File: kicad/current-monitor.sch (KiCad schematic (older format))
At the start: 4 parts, among them J1 Conn_01x02_Male, J2 Conn_01x02_Male, J3 Conn_02x05_Top_Bottom

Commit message: snapshot
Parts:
- removed J1, J2: Conn_01x02_Male, Connector_PinHeader_2.54mm:PinHeader_1x02_P2.54mm_Vertical_SMD_Pin1Left, symbol Connector:Conn_01x02_Male
- removed J3: Conn_02x05_Top_Bottom, Connector_PinHeader_2.54mm:PinHeader_2x05_P2.54mm_Vertical_SMD, symbol Connector_Generic:Conn_02x05_Top_Bottom
- added H1, H2: MountingHole, MountingHole:MountingHole_2.2mm_M2_Pad_Via, symbol Mechanical:MountingHole
- added J1, J2: Conn_02x02_Odd_Even, Connector_PinHeader_2.54mm:PinHeader_2x02_P2.54mm_Vertical_SMD, symbol Connector_Generic:Conn_02x02_Odd_Even
- added J3: Conn_02x05_Odd_Even, Connector_PinHeader_2.54mm:PinHeader_2x05_P2.54mm_Vertical_SMD, symbol Connector_Generic:Conn_02x05_Odd_Even
- added R12: 2, Resistor_SMD:R_0612_1632Metric, symbol Device:R
- R1: footprint Resistor_SMD:R_0603_1608Metric -> Resistor_SMD:R_0612_1632Metric; Description (none) -> RES SMD 2 OHM 3/4W 1206 WIDE; Digi-Key Part Number (none) -> RHM2YCT-ND; Manufacturer (none) -> Rohm Semiconductor; Manufacturer Part Number (none) -> LTR18EZPF2R00
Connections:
- net GND: now also J1.1 (Pin_1), J1.3 (Pin_3), J2.1 (Pin_1), J2.3 (Pin_3)
- net adc/3V3: now also J3.6 (Pin_6)
- net adc/CIPO: now also J3.3 (Pin_3)
- net adc/COPI: now also J3.1 (Pin_1)
- net adc/GND: now also J3.2 (Pin_2), J3.8 (Pin_8)
- net adc/SCLK: now also J3.5 (Pin_5)
- net adc/~CS: now also J3.7 (Pin_7)
- net adc/~DRDY: now also J3.9 (Pin_9)
- net adc/~SYNC: now also J3.10 (Pin_10)
- net power/5V: now also J3.4 (Pin_4)
- net sensors/S1+: now also R1.1, J1.4 (Pin_4); no longer R1.2
- net sensors/S1-: now also R1.2, J1.2 (Pin_2); no longer R1.1
- new net sensors/S3+: J2.4 (Pin_4), R12.1
- new net sensors/S3-: J2.2 (Pin_2), R12.2
- no-connect marks 2 -> 0
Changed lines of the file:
@@
 F 0 "R1" H 2320 3146 50  0000 L CNN
 F 1 "2" H 2320 3055 50  0000 L CNN
-F 2 "Resistor_SMD:R_0603_1608Metric" V 2180 3100 50  0001 C CNN
-F 3 "~" H 2250 3100 50  0001 C CNN
+F 2 "Resistor_SMD:R_0612_1632Metric" V 2180 3100 50  0001 C CNN
+F 3 "https://www.rohm.com/datasheet/LTR100JZPD/ltr-e" H 2250 3100 50  0001 C CNN
+F 4 "RHM2YCT-ND" H 2250 3100 50  0001 C CNN "Digi-Key Part Number"
+F 5 "Rohm Semiconductor" H 2250 3100 50  0001 C CNN "Manufacturer"
+F 6 "LTR18EZPF2R00" H 2250 3100 50  0001 C CNN "Manufacturer Part Number"
+F 7 "RES SMD 2 OHM 3/4W 1206 WIDE" H 2250 3100 50  0001 C CNN "Description"
 	1    2250 3100
-	1    0    0    -1
-$EndComp
-$Comp
-L Connector:Conn_01x02_Male J1
-U 1 1 5FC45001
-P 2250 2400
-F 0 "J1" V 2312 2444 50  0000 L CNN
-F 1 "Conn_01x02_Male" V 2403 2444 50  0000 L CNN
-F 2 "Connector_PinHeader_2.54mm:PinHeader_1x02_P2.54mm_Vertical_SMD_Pin1Left" H 2250 2400 50  0001 C CNN
-F 3 "~" H 2250 2400 50  0001 C CNN
-	1    2250 2400
-	0    1    1    0
-$EndComp
-$Comp
-L Connector:Conn_01x02_Male J2
-U 1 1 5FC45844
-P 2250 3750
-F 0 "J2" V 2404 3562 50  0000 R CNN
-F 1 "Conn_01x02_Male" V 2313 3562 50  0000 R CNN
-F 2 "Connector_PinHeader_2.54mm:PinHeader_1x02_P2.54mm_Vertical_SMD_Pin1Left" H 2250 3750 50  0001 C CNN
-F 3 "~" H 2250 3750 50  0001 C CNN
-	1    2250 3750
-	0    -1   -1   0
+	-1   0    0    1
 $EndComp
 Wire Wire Line
 	2250 2950 2250 2800
-Wire Wire Line
-	2250 3550 2250 3400
 Wire Wire Line
 	3050 2700 2700 2700
@@
 Connection ~ 2250 2800
 Wire Wire Line
-	2250 2800 2250 2600
-Wire Wire Line
 	2800 2800 2800 3500
 Wire Wire Line
@@
 Wire Wire Line
 	2800 2800 2250 2800
-Text Notes 2100 3950 0    50   ~ 0
+Text Notes 1800 3600 0    50   ~ 0
 Power Side
-Text Notes 2100 2250 0    50   ~ 0
+Text Notes 1850 2700 0    50   ~ 0
 Load Side
 $Comp
 L power:GND #PWR01
 U 1 1 5FC494A7
-P 1750 3100
-F 0 "#PWR01" H 1750 2850 50  0001 C CNN
-F 1 "GND" V 1755 2972 50  0000 R CNN
-F 2 "" H 1750 3100 50  0001 C CNN
-F 3 "" H 1750 3100 50  0001 C CNN
-	1    1750 3100
+P 1400 3100
+F 0 "#PWR01" H 1400 2850 50  0001 C CNN
+F 1 "GND" V 1405 2972 50  0000 R CNN
+F 2 "" H 1400 3100 50  0001 C CNN
+F 3 "" H 1400 3100 50  0001 C CNN
+	1    1400 3100
 	0    1    1    0
 $EndComp
-Wire Wire Line
-	1950 3100 1750 3100
-Wire Wire Line
-	2350 3550 2350 3500
-Wire Wire Line
-	2350 3500 1950 3500
-Wire Wire Line
-	1950 3500 1950 3100
-Wire Wire Line
-	2150 2600 2150 2650
-Wire Wire Line
-	2150 2650 1950 2650
-Wire Wire Line
-	1950 2650 1950 3100
-Connection ~ 1950 3100
 $Sheet
-S 3050 2550 1100 1000
+S 3050 2550 1150 2350
 U 5FC577BA
 F0 "sensors" 50
@@
 F4 "S2+" I L 3050 3400 50
 F5 "S2-" I L 3050 3500 50
-F6 "OUT1" I R 4150 2650 50
-F7 "GND" I R 4150 3150 50
-F8 "OUT2" I R 4150 2850 50
+F6 "OUT1" I R 4200 2650 50
+F7 "GND" I R 4200 4150 50
+F8 "OUT2" I R 4200 2850 50
+F9 "3V3" I R 4200 4350 50
+F10 "S3+" I L 3050 3900 50
+F11 "S3-" I L 3050 4000 50
+F12 "S4+" I L 3050 4600 50
+F13 "S4-" I L 3050 4700 50
+F14 "OUT3" I R 4200 3250 50
+F15 "OUT4" I R 4200 3450 50
 $EndSheet
 $Sheet
@@
 Wire Wire Line
 	8100 2200 4500 2200
-Wire Wire Line
-	4500 2200 4500 3150
-Wire Wire Line
-	4500 3150 4150 3150
 Connection ~ 8100 3100
 Wire Wire Line
 	8100 3100 8250 3100
-$Comp
-L Connector_Generic:Conn_02x05_Top_Bottom J3
-U 1 1 5FCE1CF8
+Wire Wire Line
+	6500 3700 7150 3700
+Wire Wire Line
+	6450 3850 7800 3850
+Wire Wire Line
+	7800 3850 7800 3700
+Wire Wire Line
+	7800 3700 7650 3700
+Wire Wire Line
+	6450 3600 6450 3850
+Wire Wire Line
+	7650 3500 7850 3500
+Wire Wire Line
+	7850 3500 7850 2650
+Connection ~ 7850 2650
+Wire Wire Line
+	7850 2650 6800 2650
+Wire Wire Line
+	7950 3300 7950 3600
+Wire Wire Line
+	7950 3600 7650 3600
+Connection ~ 7950 3300
+$Comp
+L Connector_Generic:Conn_02x05_Odd_Even J3
+U 1 1 5FC553C8
 P 7350 3500
 F 0 "J3" H 7400 3917 50  0000 C CNN
-F 1 "Conn_02x05_Top_Bottom" H 7400 3826 50  0000 C CNN
+F 1 "Conn_02x05_Odd_Even" H 7400 3826 50  0000 C CNN
 F 2 "Connector_PinHeader_2.54mm:PinHeader_2x05_P2.54mm_Vertical_SMD" H 7350 3500 50  0001 C CNN
 F 3 "~" H 7350 3500 50  0001 C CNN
@@
 	1    0    0    -1
 $EndComp
-Wire Wire Line
-	6500 3700 7150 3700
-Wire Wire Line
-	6450 3850 7800 3850
-Wire Wire Line
-	7800 3850 7800 3700
-Wire Wire Line
-	7800 3700 7650 3700
-Wire Wire Line
-	6450 3600 6450 3850
-Wire Wire Line
-	7650 3500 7850 3500
-Wire Wire Line
-	7850 3500 7850 2650
-Connection ~ 7850 2650
-Wire Wire Line
-	7850 2650 6250 2650
-Wire Wire Line
-	7950 3300 7950 3600
-Wire Wire Line
-	7950 3600 7650 3600
-Connection ~ 7950 3300
-NoConn ~ 5000 3250
-NoConn ~ 5000 3450
+$Comp
+L Connector_Generic:Conn_02x02_Odd_Even J1
+U 1 1 5FC56274
+P 1700 3050
+F 0 "J1" V 1750 3130 50  0000 L CNN
+F 1 "Conn_02x02_Odd_Even" V 1795 3130 50  0001 L CNN
+F 2 "Connector_PinHeader_2.54mm:PinHeader_2x02_P2.54mm_Vertical_SMD" H 1700 3050 50  0001 C CNN
+F 3 "~" H 1700 3050 50  0001 C CNN
+	1    1700 3050
+	1    0    0    -1
+$EndComp
+$Comp
+L Mechanical:MountingHole H2
+U 1 1 5FC83785
+P 1350 5600
+F 0 "H2" H 1450 5646 50  0000 L CNN
+F 1 "MountingHole" H 1450 5555 50  0000 L CNN
+F 2 "MountingHole:MountingHole_2.2mm_M2_Pad_Via" H 1350 5600 50  0001 C CNN
+F 3 "~" H 1350 5600 50  0001 C CNN
+	1    1350 5600
+	1    0    0    -1
+$EndComp
+$Comp
+L Mechanical:MountingHole H1
+U 1 1 5FC83AA2
+P 1350 5400
+F 0 "H1" H 1450 5446 50  0000 L CNN
+F 1 "MountingHole" H 1450 5355 50  0000 L CNN
+F 2 "MountingHole:MountingHole_2.2mm_M2_Pad_Via" H 1350 5400 50  0001 C CNN
+F 3 "~" H 1350 5400 50  0001 C CNN
+	1    1350 5400
+	1    0    0    -1
+$EndComp
+Wire Wire Line
+	2000 2800 2000 3050
+Wire Wire Line
+	2000 2800 2250 2800
+Wire Wire Line
+	2000 3400 2000 3150
+Wire Wire Line
+	2000 3400 2250 3400
+Wire Wire Line
+	1500 3050 1400 3050
+Wire Wire Line
+	1400 3050 1400 3100
+Wire Wire Line
+	1500 3150 1400 3150
+Wire Wire Line
+	1400 3150 1400 3100
+Connection ~ 1400 3100
+$Comp
+L Device:R R12
+U 1 1 5FC968B8
+P 2250 4300
+F 0 "R12" H 2320 4346 50  0000 L CNN
+F 1 "2" H 2320 4255 50  0000 L CNN
+F 2 "Resistor_SMD:R_0612_1632Metric" V 2180 4300 50  0001 C CNN
+F 3 "https://www.rohm.com/datasheet/LTR100JZPD/ltr-e" H 2250 4300 50  0001 C CNN
+F 4 "RHM2YCT-ND" H 2250 4300 50  0001 C CNN "Digi-Key Part Number"
+F 5 "Rohm Semiconductor" H 2250 4300 50  0001 C CNN "Manufacturer"
+F 6 "LTR18EZPF2R00" H 2250 4300 50  0001 C CNN "Manufacturer Part Number"
+F 7 "RES SMD 2 OHM 3/4W 1206 WIDE" H 2250 4300 50  0001 C CNN "Description"
+	1    2250 4300
+	-1   0    0    1
+$EndComp
+Wire Wire Line
+	2250 4150 2250 4000
+Wire Wire Line
+	2700 4600 2250 4600
+Connection ~ 2250 4600
+Wire Wire Line
+	2250 4600 2250 4450
+Connection ~ 2250 4000
+Wire Wire Line
+	2800 4000 2250 4000
+Text Notes 1800 4800 0    50   ~ 0
+Power Side
+Text Notes 1850 3900 0    50   ~ 0
+Load Side
+$Comp
+L power:GND #PWR02
+U 1 1 5FC9691A
+P 1400 4300
+F 0 "#PWR02" H 1400 4050 50  0001 C CNN
+F 1 "GND" V 1405 4172 50  0000 R CNN
+F 2 "" H 1400 4300 50  0001 C CNN
+F 3 "" H 1400 4300 50  0001 C CNN
+	1    1400 4300
+	0    1    1    0
+$EndComp
+$Comp
+L Connector_Generic:Conn_02x02_Odd_Even J2
+U 1 1 5FC96924
+P 1700 4250
+F 0 "J2" V 1750 4330 50  0000 L CNN
+F 1 "Conn_02x02_Odd_Even" V 1795 4330 50  0001 L CNN
+F 2 "Connector_PinHeader_2.54mm:PinHeader_2x02_P2.54mm_Vertical_SMD" H 1700 4250 50  0001 C CNN
+F 3 "~" H 1700 4250 50  0001 C CNN
+	1    1700 4250
+	1    0    0    -1
+$EndComp
+Wire Wire Line
+	2000 4000 2000 4250
+Wire Wire Line
+	2000 4000 2250 4000
+Wire Wire Line
+	2000 4600 2000 4350
+Wire Wire Line
+	2000 4600 2250 4600
+Wire Wire Line
+	1500 4250 1400 4250
+Wire Wire Line
+	1400 4250 1400 4300
+Wire Wire Line
+	1500 4350 1400 4350
+Wire Wire Line
+	1400 4350 1400 4300
+Connection ~ 1400 4300
+Wire Wire Line
+	4500 4150 4200 4150
+Wire Wire Line
+	4500 2200 4500 4150
+Wire Wire Line
+	6800 2650 6800 2250
+Wire Wire Line
+	6800 2250 4550 2250
+Wire Wire Line
+	4550 2250 4550 4350
+Wire Wire Line
+	4550 4350 4200 4350
+Connection ~ 6800 2650
+Wire Wire Line
+	6800 2650 6250 2650
+Wire Wire Line
+	4200 3250 5000 3250
+Wire Wire Line
+	5000 3450 4200 3450
+Wire Wire Line
+	2800 4000 2800 4700
+Wire Wire Line
+	2800 4700 3050 4700
+Wire Wire Line
+	2800 4000 3050 4000
+Connection ~ 2800 4000
+Wire Wire Line
+	2700 4600 2700 3900
+Wire Wire Line
+	2700 3900 3050 3900
+Wire Wire Line
+	2700 4600 3050 4600
+Connection ~ 2700 4600
 $EndSCHEMATC

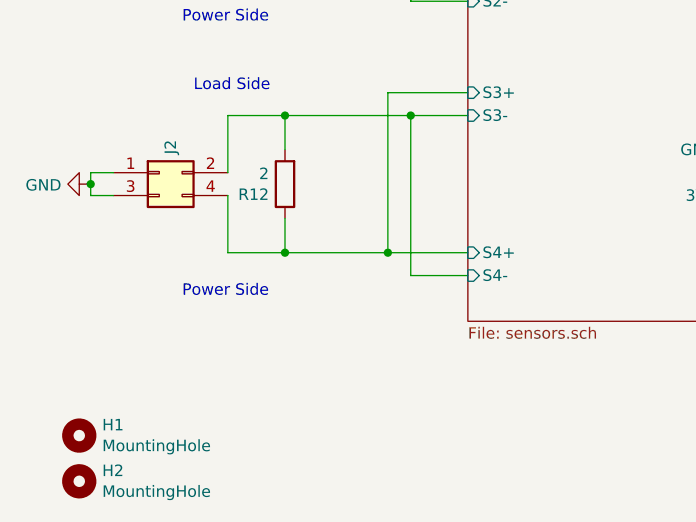
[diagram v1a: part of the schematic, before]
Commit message: add second R_sense
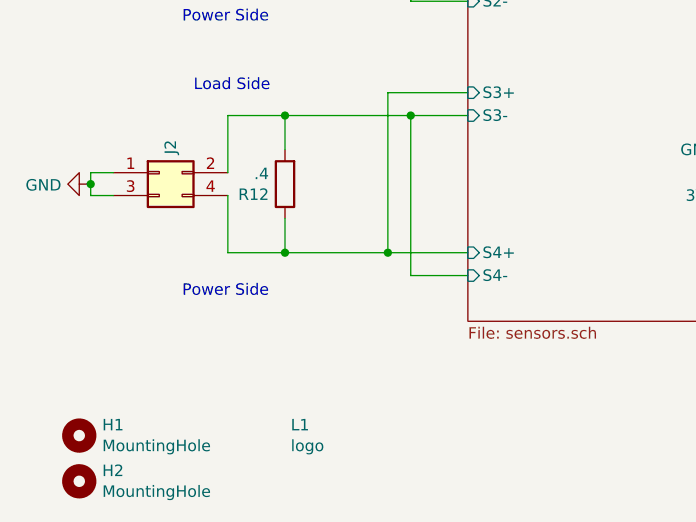
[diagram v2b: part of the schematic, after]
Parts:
- added L1: logo, HH_Hochreiner:logo, symbol HH_Hochreiner:logo
- R12: value 2 -> .4; footprint Resistor_SMD:R_0612_1632Metric -> Resistor_SMD:R_2010_5025Metric; Description RES SMD 2 OHM 3/4W 1206 WIDE -> RES 0.4 OHM 1% 1W 2010; Digi-Key Part Number RHM2YCT-ND -> WSLTA-.400CT-ND; Manufacturer Rohm Semiconductor -> Vishay Dale; Manufacturer Part Number LTR18EZPF2R00 -> WSLT2010R4000FEB18
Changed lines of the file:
@@
 P 2250 4300
 F 0 "R12" H 2320 4346 50  0000 L CNN
-F 1 "2" H 2320 4255 50  0000 L CNN
-F 2 "Resistor_SMD:R_0612_1632Metric" V 2180 4300 50  0001 C CNN
-F 3 "https://www.rohm.com/datasheet/LTR100JZPD/ltr-e" H 2250 4300 50  0001 C CNN
-F 4 "RHM2YCT-ND" H 2250 4300 50  0001 C CNN "Digi-Key Part Number"
-F 5 "Rohm Semiconductor" H 2250 4300 50  0001 C CNN "Manufacturer"
-F 6 "LTR18EZPF2R00" H 2250 4300 50  0001 C CNN "Manufacturer Part Number"
-F 7 "RES SMD 2 OHM 3/4W 1206 WIDE" H 2250 4300 50  0001 C CNN "Description"
+F 1 ".4" H 2320 4255 50  0000 L CNN
+F 2 "Resistor_SMD:R_2010_5025Metric" V 2180 4300 50  0001 C CNN
+F 3 "https://www.vishay.com/docs/30138/wslt2010.pdf" H 2250 4300 50  0001 C CNN
+F 4 "WSLTA-.400CT-ND" H 2250 4300 50  0001 C CNN "Digi-Key Part Number"
+F 5 "Vishay Dale" H 2250 4300 50  0001 C CNN "Manufacturer"
+F 6 "WSLT2010R4000FEB18" H 2250 4300 50  0001 C CNN "Manufacturer Part Number"
+F 7 "RES 0.4 OHM 1% 1W 2010" H 2250 4300 50  0001 C CNN "Description"
 	1    2250 4300
 	-1   0    0    1
@@
 	2700 4600 3050 4600
 Connection ~ 2700 4600
+$Comp
+L HH_Hochreiner:logo L1
+U 1 1 5FC9FF08
+P 2250 5400
+F 0 "L1" H 2275 5446 50  0000 L CNN
+F 1 "logo" H 2275 5355 50  0000 L CNN
+F 2 "HH_Hochreiner:logo" H 2150 5250 50  0001 C CNN
+F 3 "" H 2250 5400 50  0001 C CNN
+	1    2250 5400
+	1    0    0    -1
+$EndComp
 $EndSCHEMATC

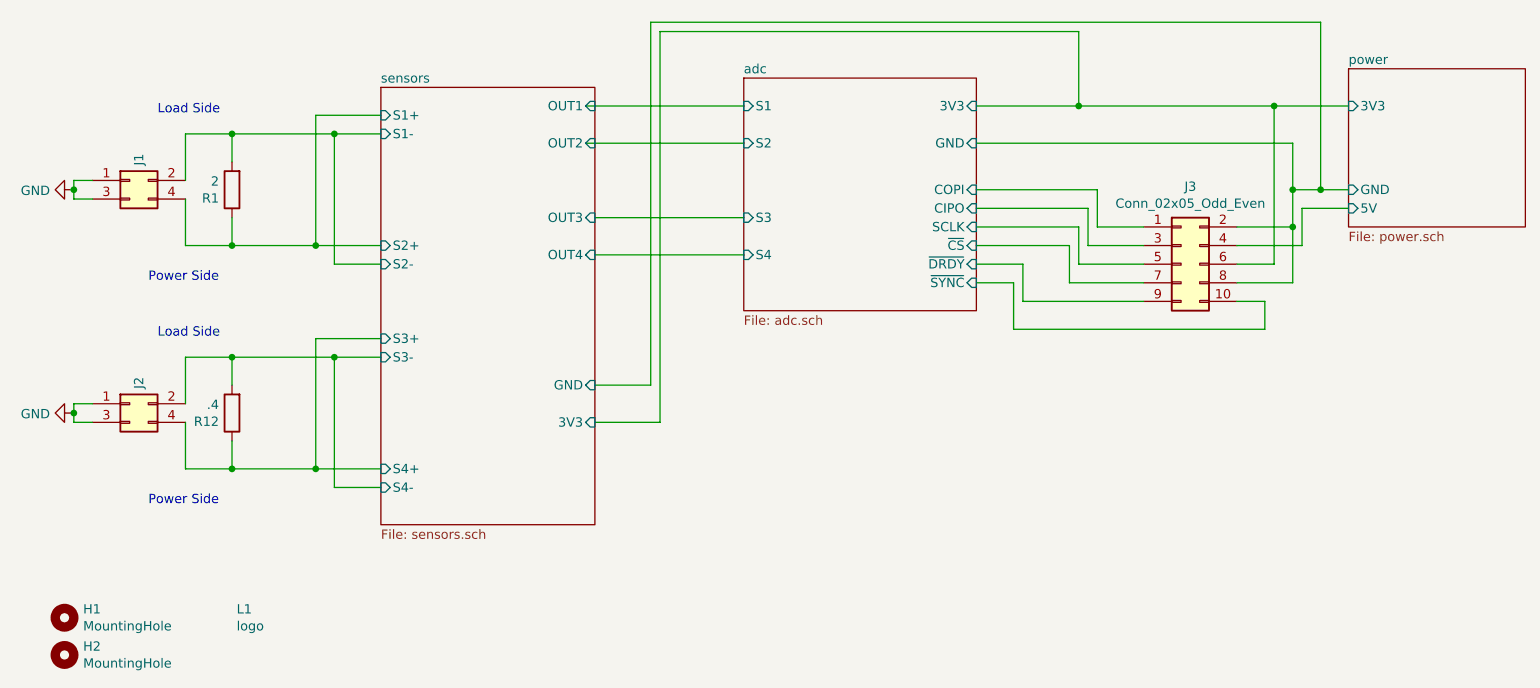
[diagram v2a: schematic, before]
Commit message: move clock to back
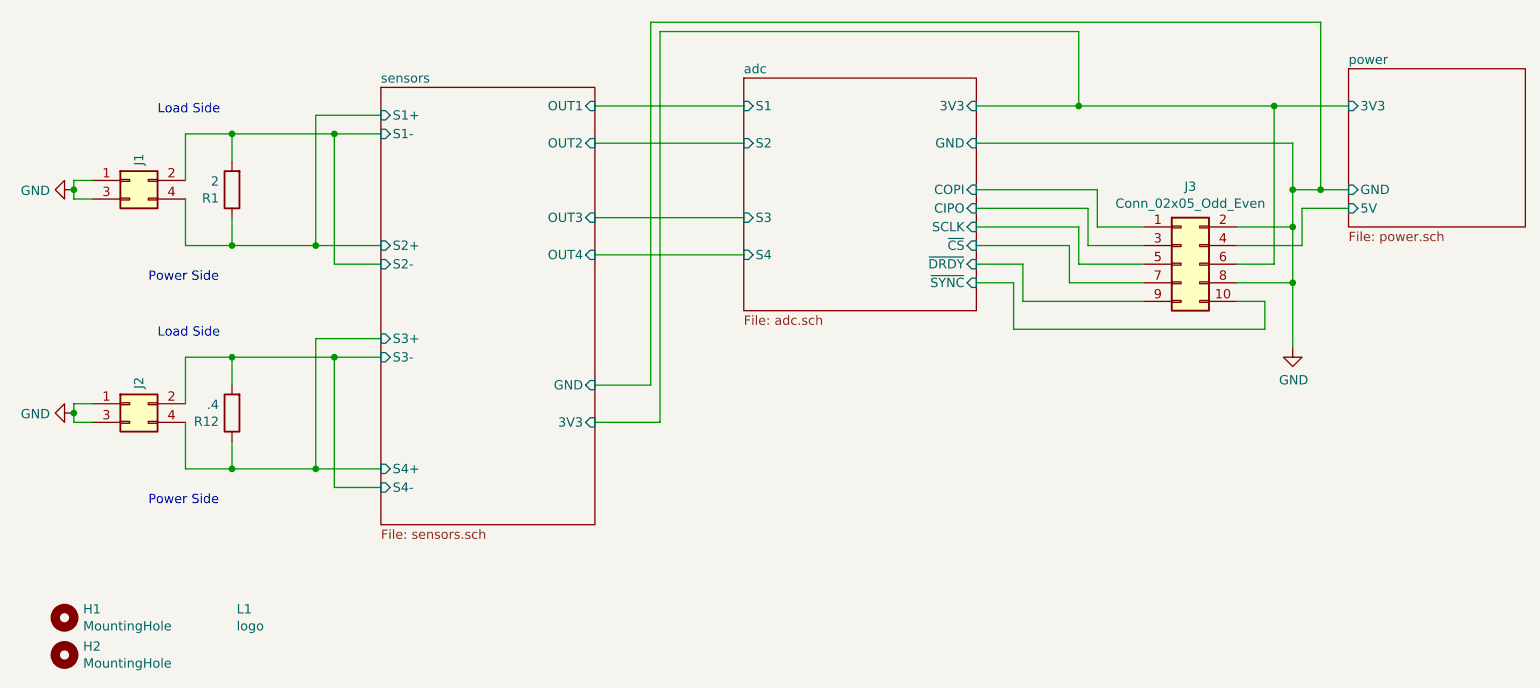
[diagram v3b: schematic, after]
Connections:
- net adc/GND is gone; now on net GND: J3.2 (Pin_2), J3.8 (Pin_8)
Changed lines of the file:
@@
 F13 "~SYNC" I R 6250 3600 50
 $EndSheet
-Wire Wire Line
-	4150 2650 5000 2650
-Wire Wire Line
-	4150 2850 5000 2850
 $Sheet
 S 8250 2450 950  850
@@
 	1    0    0    -1
 $EndComp
+Wire Wire Line
+	4200 2650 5000 2650
+Wire Wire Line
+	4200 2850 5000 2850
+$Comp
+L power:GND #PWR?
+U 1 1 5FCBC214
+P 7950 3950
+F 0 "#PWR?" H 7950 3700 50  0001 C CNN
+F 1 "GND" H 7955 3777 50  0000 C CNN
+F 2 "" H 7950 3950 50  0001 C CNN
+F 3 "" H 7950 3950 50  0001 C CNN
+	1    7950 3950
+	1    0    0    -1
+$EndComp
+Wire Wire Line
+	7950 3950 7950 3600
+Connection ~ 7950 3600
 $EndSCHEMATC

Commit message: put markings on pcb
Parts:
- J3: Description (none) -> CONN HEADER SMD 10POS 2.54MM; Digi-Key Part Number (none) -> 609-10129383-910002ALFCT-ND; Manufacturer (none) -> Amphenol ICC (FCI); Manufacturer Part Number (none) -> 10129383-910002ALF
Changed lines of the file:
@@
 F 1 "Conn_02x05_Odd_Even" H 7400 3826 50  0000 C CNN
 F 2 "Connector_PinHeader_2.54mm:PinHeader_2x05_P2.54mm_Vertical_SMD" H 7350 3500 50  0001 C CNN
-F 3 "~" H 7350 3500 50  0001 C CNN
+F 3 "https://cdn.amphenol-icc.com/media/wysiwyg/files/drawing/10129383.pdf?__cf_chl_jschl_tk__=50692e9c3c7b852df7b3b370973279a538e8a103-1607200140-0-AWM_6pj0I2i4US69aCDIx512BmlW4S-DDul6dgsnJetJD-IqebQ1U7662gPUjtX4C-S0USluXoTJcEGbWi8i_3rpM9Pjf5hMxeXBx247_wzmnS6DcJj7LzOJKMRZ_CFUApRYpPD3fsZRJMNRugg3LtyvUTA0mO38lDevQ7vFgr71JWlgRNsJESWDCg1jfFl5DNg5-YjNqITQVhFagICPMOM1XaUroWIxlHQ5h1lny7pTfF_YMnFHf2AZHswAe7u9CV314bmkbACIwQu8EPCHW1kibxxmg3D15jSVsCDKcKZ1KpEk36t1kWYOzxj5vtJncrQcc8AzjPyVpD5pOkVEurCbvD1ozvf7agNQNgik5j64WJTEOBLmWB9-Ts3O92zFZYGPkG9knV4v2QwhZGDJuzp5fYi-Rj_qR5JrUHbP3Lqy" H 7350 3500 50  0001 C CNN
+F 4 "609-10129383-910002ALFCT-ND" H 7350 3500 50  0001 C CNN "Digi-Key Part Number"
+F 5 "Amphenol ICC (FCI)" H 7350 3500 50  0001 C CNN "Manufacturer"
+F 6 "10129383-910002ALF" H 7350 3500 50  0001 C CNN "Manufacturer Part Number"
+F 7 "CONN HEADER SMD 10POS 2.54MM" H 7350 3500 50  0001 C CNN "Description"
 	1    7350 3500
 	1    0    0    -1
